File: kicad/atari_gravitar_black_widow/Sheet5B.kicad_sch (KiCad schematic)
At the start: 23 parts

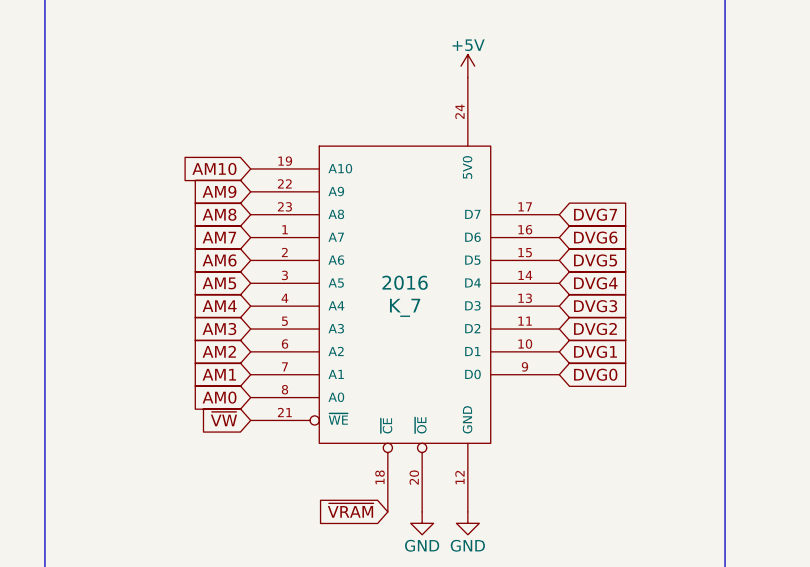
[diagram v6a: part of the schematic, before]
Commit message: more chip layouts
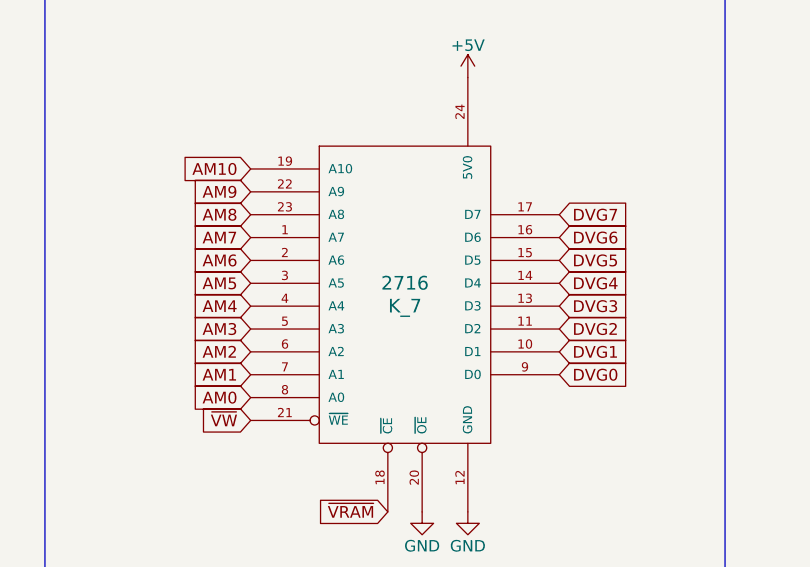
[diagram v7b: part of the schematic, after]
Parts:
- J_3, J_6: footprint (none) -> Star_Wars_Vector_PCB:DIP14
- J_7, K_8: footprint (none) -> Star_Wars_Vector_PCB:DIP16
- K_7: value 2016 -> 2716; footprint (none) -> Star_Wars_Vector_PCB:DDIP24
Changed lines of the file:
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@@
       (effects (font (size 1.524 1.524)))
     )
-    (property "Value" "2016" (id 1) (at 220.345 176.53 0)
+    (property "Value" "2716" (id 1) (at 220.345 176.53 0)
       (effects (font (size 1.524 1.524)))
     )
-    (property "Footprint" "" (id 2) (at 221.615 180.34 0)
+    (property "Footprint" "Star_Wars_Vector_PCB:DDIP24" (id 2) (at 221.615 180.34 0)
       (effects (font (size 1.524 1.524)) hide)
     )
@@
       (effects (font (size 1.27 1.27)) (justify left))
     )
-    (property "Footprint" "" (id 2) (at 69.215 180.975 0)
+    (property "Footprint" "Star_Wars_Vector_PCB:DIP16" (id 2) (at 69.215 180.975 0)
       (effects (font (size 1.27 1.27)) hide)
     )
@@
       (effects (font (size 1.27 1.27)) (justify left))
     )
-    (property "Footprint" "" (id 2) (at 93.98 98.425 0)
+    (property "Footprint" "Star_Wars_Vector_PCB:DIP16" (id 2) (at 93.98 98.425 0)
       (effects (font (size 1.27 1.27)) hide)
     )
@@
     (property "Reference" "J_7" (id 0) (at 78.105 64.643 0))
     (property "Value" "LS139" (id 1) (at 78.232 67.818 0))
-    (property "Footprint" "" (id 2) (at 78.74 67.31 0)
+    (property "Footprint" "Star_Wars_Vector_PCB:DIP16" (id 2) (at 78.74 67.31 0)
       (effects (font (size 1.27 1.27)) hide)
     )
@@
     (property "Reference" "J_3" (id 0) (at 104.013 234.188 0))
     (property "Value" "LS04" (id 1) (at 104.013 236.093 0))
-    (property "Footprint" "" (id 2) (at 105.283 234.823 0)
+    (property "Footprint" "Star_Wars_Vector_PCB:DIP14" (id 2) (at 105.283 234.823 0)
       (effects (font (size 1.27 1.27)) hide)
     )
@@
     (property "Reference" "J_6" (id 0) (at 126.365 167.005 0))
     (property "Value" "LS32" (id 1) (at 126.365 168.91 0))
-    (property "Footprint" "" (id 2) (at 126.365 168.275 0)
-      (effects (font (size 1.27 1.27)) hide)
-    )
+    (property "Footprint" "Star_Wars_Vector_PCB:DIP14" (id 2) (at 126.365 168.275 0)
+      (effects (font (size 1.27 1.27)) hide)
+    )

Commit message: placements
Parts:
- L_7, M/N_7, N/P_7, R_7: footprint (none) -> Star_Wars_Vector_PCB:DDIP24
- L_8, M_8, N_8: footprint (none) -> Star_Wars_Vector_PCB:DIP16
- M_5: footprint (none) -> Star_Wars_Vector_PCB:DIP14
- P_8: footprint (none) -> Star_Wars_Vector_PCB:DIP20
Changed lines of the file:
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@@
       (effects (font (size 1.27 1.27)) (justify left))
     )
-    (property "Footprint" "" (id 2) (at 196.85 70.485 0)
+    (property "Footprint" "Star_Wars_Vector_PCB:DDIP24" (id 2) (at 196.85 70.485 0)
       (effects (font (size 1.27 1.27)) hide)
     )
@@
       (effects (font (size 1.27 1.27)) (justify left))
     )
-    (property "Footprint" "" (id 2) (at 70.485 361.95 0)
+    (property "Footprint" "Star_Wars_Vector_PCB:DIP16" (id 2) (at 70.485 361.95 0)
       (effects (font (size 1.27 1.27)) hide)
     )
@@
       (effects (font (size 1.27 1.27)) (justify left))
     )
-    (property "Footprint" "" (id 2) (at 70.485 307.975 0)
+    (property "Footprint" "Star_Wars_Vector_PCB:DIP16" (id 2) (at 70.485 307.975 0)
       (effects (font (size 1.27 1.27)) hide)
     )
@@
       (effects (font (size 1.27 1.27)) (justify left))
     )
-    (property "Footprint" "" (id 2) (at 260.35 70.485 0)
+    (property "Footprint" "Star_Wars_Vector_PCB:DDIP24" (id 2) (at 260.35 70.485 0)
       (effects (font (size 1.27 1.27)) hide)
     )
@@
       (effects (font (size 1.27 1.27)) (justify left))
     )
-    (property "Footprint" "" (id 2) (at 387.35 71.755 0)
+    (property "Footprint" "Star_Wars_Vector_PCB:DDIP24" (id 2) (at 387.35 71.755 0)
       (effects (font (size 1.27 1.27)) hide)
     )
@@
       (effects (font (size 1.27 1.27)) (justify left))
     )
-    (property "Footprint" "" (id 2) (at 525.145 73.025 0)
+    (property "Footprint" "Star_Wars_Vector_PCB:DIP20" (id 2) (at 525.145 73.025 0)
       (effects (font (size 1.27 1.27)) hide)
     )
@@
       (effects (font (size 1.27 1.27)) (justify left))
     )
-    (property "Footprint" "" (id 2) (at 69.215 247.015 0)
+    (property "Footprint" "Star_Wars_Vector_PCB:DIP16" (id 2) (at 69.215 247.015 0)
       (effects (font (size 1.27 1.27)) hide)
     )
@@
       (effects (font (size 1.27 1.27)) (justify left))
     )
-    (property "Footprint" "" (id 2) (at 323.85 70.485 0)
+    (property "Footprint" "Star_Wars_Vector_PCB:DDIP24" (id 2) (at 323.85 70.485 0)
       (effects (font (size 1.27 1.27)) hide)
     )
@@
     (property "Reference" "M_5" (id 0) (at 127.635 226.06 0))
     (property "Value" "LS32" (id 1) (at 127.254 229.743 0))
-    (property "Footprint" "" (id 2) (at 127.635 227.33 0)
-      (effects (font (size 1.27 1.27)) hide)
-    )
+    (property "Footprint" "Star_Wars_Vector_PCB:DIP14" (id 2) (at 127.635 227.33 0)
+      (effects (font (size 1.27 1.27)) hide)
+    )
